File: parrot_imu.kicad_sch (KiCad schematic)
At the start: 1 part

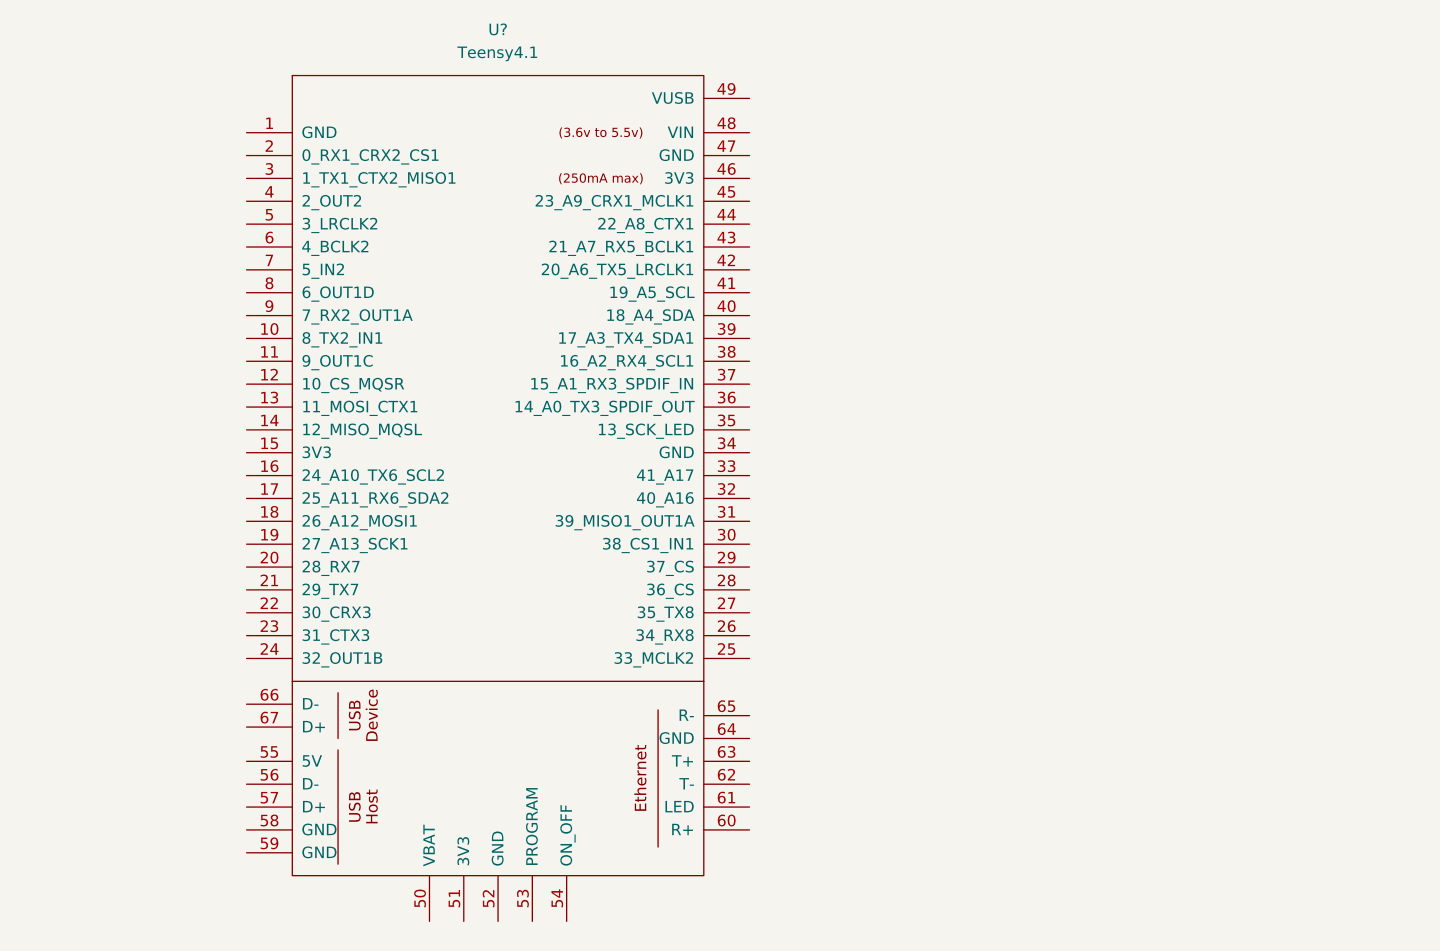
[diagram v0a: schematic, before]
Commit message: added ethernet jack symbol
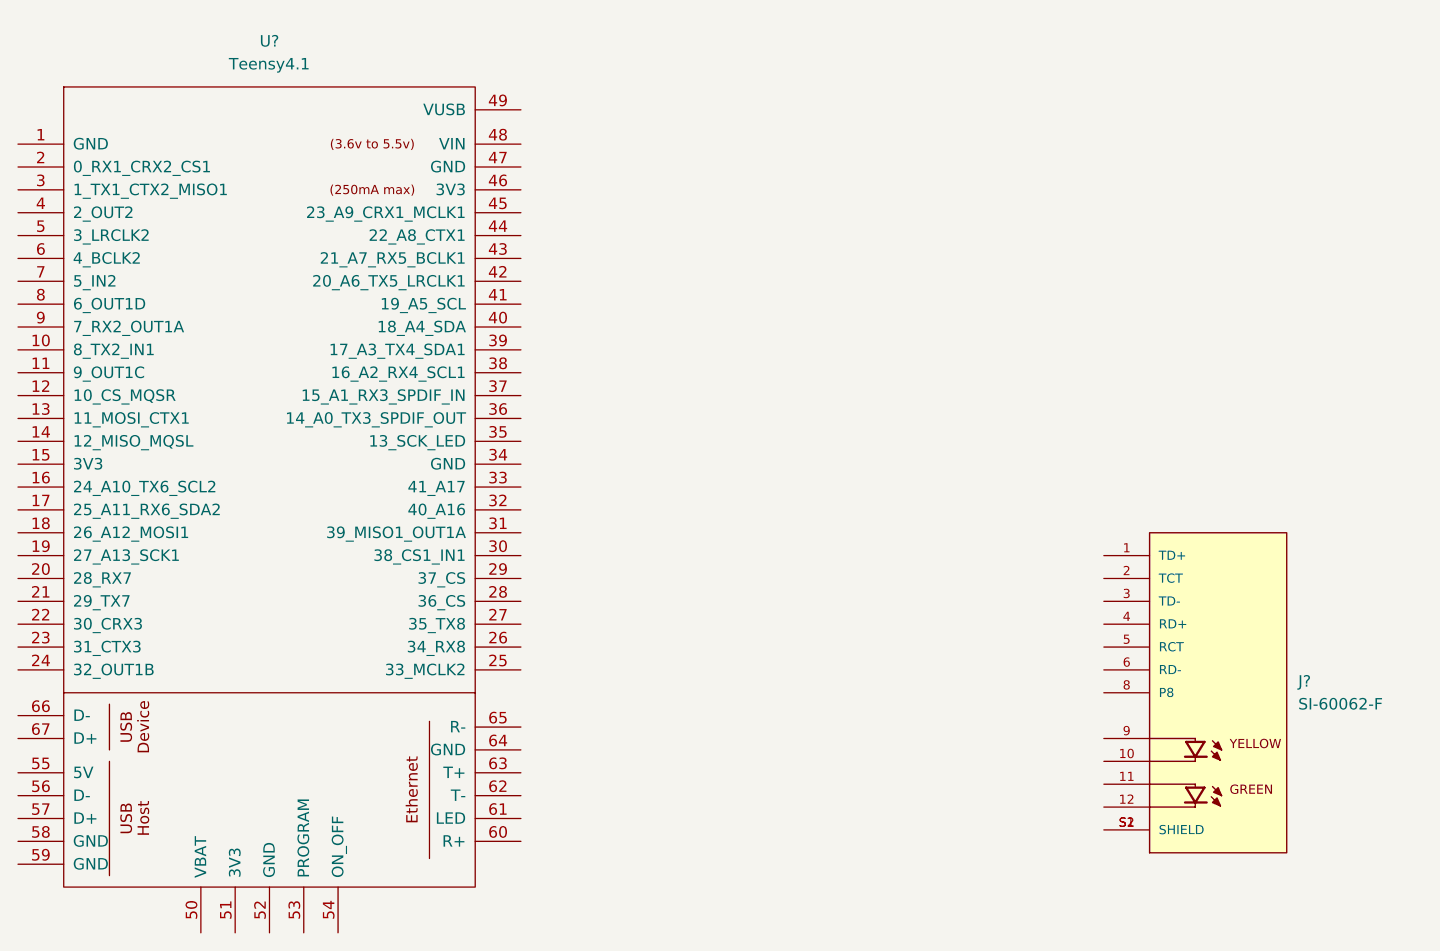
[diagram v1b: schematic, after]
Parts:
- added J?: SI-60062-F, Connector_RJ:RJ45_Bel_SI-60062-F, symbol SI-60062-F:SI-60062-F
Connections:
- new net: J?.S1 (SHIELD), J?.S2 (SHIELD)
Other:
- moved on the sheet: U?
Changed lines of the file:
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@@
 (kicad_sch (version 20211123) (generator eeschema)
   (paper "A4")
-  (symbol (lib_id "teensy_symbol:Teensy4.1") (at 144.78 97.79 0) (unit 1)
+  (symbol (lib_id "teensy_symbol:Teensy4.1") (at 119.38 99.06 0) (unit 1)
     (in_bom yes) (on_board yes) (fields_autoplaced)
-    (property "Reference" "U?" (id 0) (at 144.78 31.75 0))
-    (property "Value" "Teensy4.1" (id 1) (at 144.78 34.29 0))
-    (property "Footprint" "teensy_footprint:Teensy41" (id 2) (at 134.62 87.63 0)
+    (property "Reference" "U?" (id 0) (at 119.38 33.02 0))
+    (property "Value" "Teensy4.1" (id 1) (at 119.38 35.56 0))
+    (property "Footprint" "teensy_footprint:Teensy41" (id 2) (at 109.22 88.9 0)
       (effects (font (size 1.27 1.27)) hide)
     )
-    (property "Datasheet" "" (id 3) (at 134.62 87.63 0)
+    (property "Datasheet" "" (id 3) (at 109.22 88.9 0)
       (effects (font (size 1.27 1.27)) hide)
     )
@@
     (pin "4")
   )
+  (symbol (lib_id "SI-60062-F:SI-60062-F") (at 224.79 105.41 0) (unit 1)
+    (in_bom yes) (on_board yes) (fields_autoplaced)
+    (property "Reference" "J?" (id 0) (at 233.68 104.1399 0)
+      (effects (font (size 1.27 1.27)) (justify left))
+    )
+    (property "Value" "SI-60062-F" (id 1) (at 233.68 106.6799 0)
+      (effects (font (size 1.27 1.27)) (justify left))
+    )
+    (property "Footprint" "Connector_RJ:RJ45_Bel_SI-60062-F" (id 2) (at 224.79 105.41 0)
+      (effects (font (size 1.27 1.27)) (justify bottom) hide)
+    )
+    (property "Datasheet" "" (id 3) (at 224.79 105.41 0)
+      (effects (font (size 1.27 1.27)) hide)
+    )
+    (property "STANDARD" "Manufacturer Recommendations" (id 4) (at 224.79 105.41 0)
+      (effects (font (size 1.27 1.27)) (justify bottom) hide)
+    )
+    (property "MAXIMUM_PACKAGE_HEIGHT" "15.21mm" (id 5) (at 224.79 105.41 0)
+      (effects (font (size 1.27 1.27)) (justify bottom) hide)
+    )
+    (property "MANUFACTURER" "Bel Fuse" (id 6) (at 224.79 105.41 0)
+      (effects (font (size 1.27 1.27)) (justify bottom) hide)
+    )
+    (property "PARTREV" "B0" (id 7) (at 224.79 105.41 0)
+      (effects (font (size 1.27 1.27)) (justify bottom) hide)
+    )
+    (pin "1")
+    (pin "10")
+    (pin "11")
+    (pin "12")
+    (pin "2")
+    (pin "3")
+    (pin "4")
+    (pin "5")
+    (pin "6")
+    (pin "8")
+    (pin "9")
+    (pin "S1")
+    (pin "S2")
+  )
   (sheet_instances
     (path "/" (page "1"))
   )
   (symbol_instances
+    (path "/ee96e4e8-cf28-4230-aa42-258281590056"
+      (reference "J?") (unit 1) (value "SI-60062-F") (footprint "Connector_RJ:RJ45_Bel_SI-60062-F")
+    )
     (path "/cc736701-b530-419e-931a-68b81ff9c957"
       (reference "U?") (unit 1) (value "Teensy4.1") (footprint "teensy_footprint:Teensy41")

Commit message: added digikey part number to ethernet part
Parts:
- J?: Digikey (none) -> 507-SI-60062-F-ND
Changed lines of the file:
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@@
       (effects (font (size 1.27 1.27)) (justify bottom) hide)
+    )
+    (property "Digikey" "507-SI-60062-F-ND" (id 8) (at 224.79 105.41 0)
+      (effects (font (size 1.27 1.27)) hide)
     )
     (pin "1")

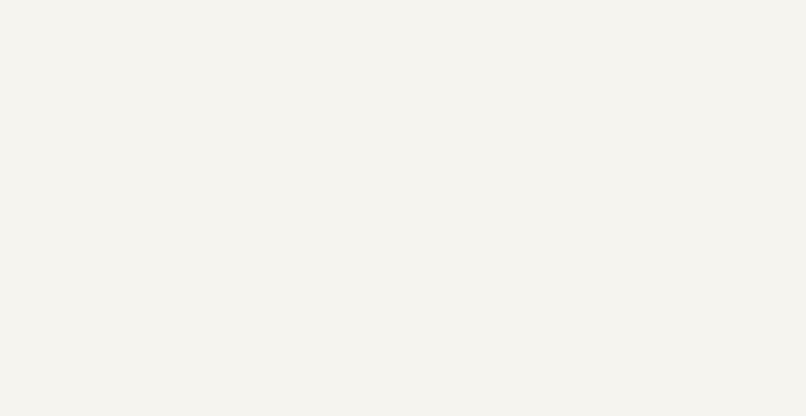
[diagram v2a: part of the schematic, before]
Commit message: created footprint and symbol for ldo
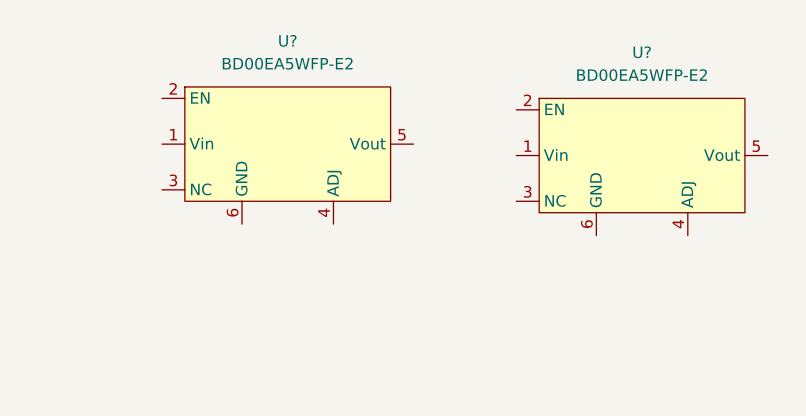
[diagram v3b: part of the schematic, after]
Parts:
- added U? (x2): BD00EA5WFP-E2, parrot_imu:BD00EA5WFP-E2, symbol parrot_imu:BD00EA5WFP-E2
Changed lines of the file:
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@@
 (kicad_sch (version 20211123) (generator eeschema)
   (paper "A4")
+  (symbol (lib_id "parrot_imu:BD00EA5WFP-E2") (at 231.14 46.99 0) (unit 1)
+    (in_bom yes) (on_board yes) (fields_autoplaced)
+    (property "Reference" "U?" (id 0) (at 231.14 35.56 0))
+    (property "Value" "BD00EA5WFP-E2" (id 1) (at 231.14 38.1 0))
+    (property "Footprint" "parrot_imu:BD00EA5WFP-E2" (id 2) (at 231.14 31.75 0)
+      (effects (font (size 1.27 1.27)) hide)
+    )
+    (property "Datasheet" "" (id 3) (at 231.14 46.99 0)
+      (effects (font (size 1.27 1.27)) hide)
+    )
+    (property "Digikey" "846-BD00EA5WFP-E2CT-ND" (id 4) (at 231.14 34.29 0)
+      (effects (font (size 1.27 1.27)) hide)
+    )
+    (pin "1")
+    (pin "2")
+    (pin "3")
+    (pin "4")
+    (pin "5")
+    (pin "6")
+  )
+  (symbol (lib_id "parrot_imu:BD00EA5WFP-E2") (at 191.77 45.72 0) (unit 1)
+    (in_bom yes) (on_board yes) (fields_autoplaced)
+    (property "Reference" "U?" (id 0) (at 191.77 34.29 0))
+    (property "Value" "BD00EA5WFP-E2" (id 1) (at 191.77 36.83 0))
+    (property "Footprint" "parrot_imu:BD00EA5WFP-E2" (id 2) (at 191.77 30.48 0)
+      (effects (font (size 1.27 1.27)) hide)
+    )
+    (property "Datasheet" "" (id 3) (at 191.77 45.72 0)
+      (effects (font (size 1.27 1.27)) hide)
+    )
+    (property "Digikey" "846-BD00EA5WFP-E2CT-ND" (id 4) (at 191.77 33.02 0)
+      (effects (font (size 1.27 1.27)) hide)
+    )
+    (pin "1")
+    (pin "2")
+    (pin "3")
+    (pin "4")
+    (pin "5")
+    (pin "6")
+  )
   (symbol (lib_id "teensy_symbol:Teensy4.1") (at 119.38 99.06 0) (unit 1)
     (in_bom yes) (on_board yes) (fields_autoplaced)
@@
       (reference "J?") (unit 1) (value "SI-60062-F") (footprint "Connector_RJ:RJ45_Bel_SI-60062-F")
     )
+    (path "/77c37afd-a1ed-485e-8b5f-ecf763893ed1"
+      (reference "U?") (unit 1) (value "BD00EA5WFP-E2") (footprint "parrot_imu:BD00EA5WFP-E2")
+    )
+    (path "/9cadbf9f-a3bf-4ef2-ad9b-3cea417c0dcf"
+      (reference "U?") (unit 1) (value "BD00EA5WFP-E2") (footprint "parrot_imu:BD00EA5WFP-E2")
+    )
     (path "/cc736701-b530-419e-931a-68b81ff9c957"

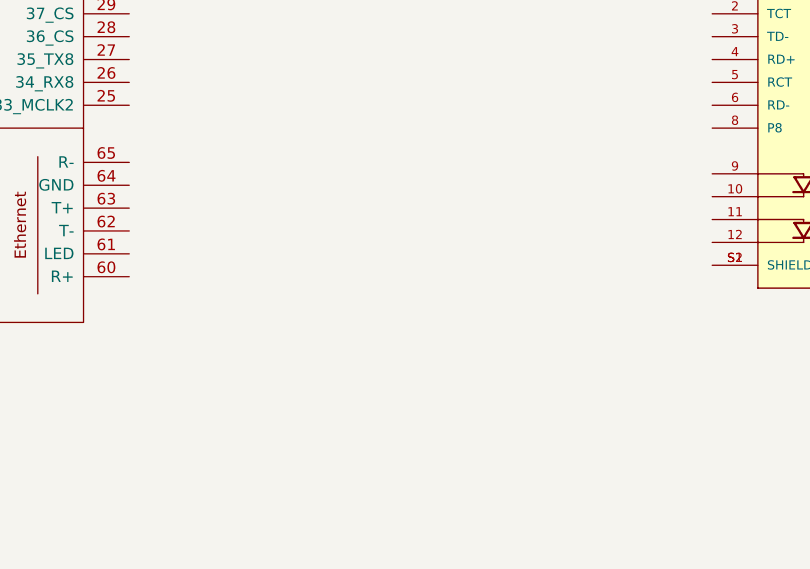
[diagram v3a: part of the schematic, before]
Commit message: added ics to schematic
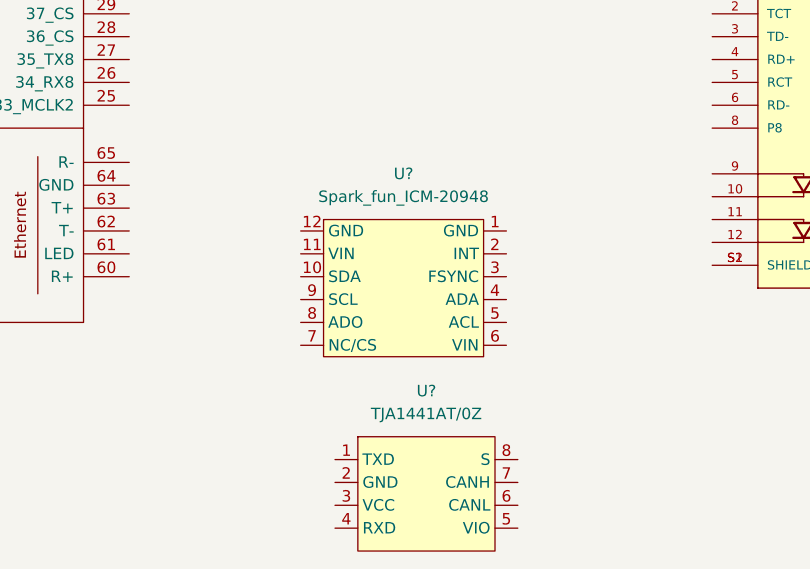
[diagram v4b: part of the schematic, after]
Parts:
- added U?: TJA1441AT/0Z, Package_SO:SO-8_3.9x4.9mm_P1.27mm, symbol parrot_imu:TJA1441AT/0Z
- added U?: Spark_fun_ICM-20948, parrot_imu:Spark_fun_ICM-20498, symbol parrot_imu:Spark_fun_ICM-20948
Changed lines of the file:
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@@
     (pin "6")
+  )
+  (symbol (lib_id "parrot_imu:TJA1441AT{slash}0Z") (at 180.34 146.05 0) (unit 1)
+    (in_bom yes) (on_board yes) (fields_autoplaced)
+    (property "Reference" "U?" (id 0) (at 180.34 134.62 0))
+    (property "Value" "TJA1441AT/0Z" (id 1) (at 180.34 137.16 0))
+    (property "Footprint" "Package_SO:SO-8_3.9x4.9mm_P1.27mm" (id 2) (at 180.34 135.89 0)
+      (effects (font (size 1.27 1.27)) hide)
+    )
+    (property "Datasheet" "" (id 3) (at 180.34 146.05 0)
+      (effects (font (size 1.27 1.27)) hide)
+    )
+    (property "Digikey" "568-TJA1441AT/0ZCT-ND" (id 4) (at 180.34 133.35 0)
+      (effects (font (size 1.27 1.27)) hide)
+    )
+    (pin "1")
+    (pin "2")
+    (pin "3")
+    (pin "4")
+    (pin "5")
+    (pin "6")
+    (pin "7")
+    (pin "8")
   )
   (symbol (lib_id "parrot_imu:BD00EA5WFP-E2") (at 191.77 45.72 0) (unit 1)
@@
     (pin "S2")
   )
+  (symbol (lib_id "parrot_imu:Spark_fun_ICM-20948") (at 177.8 123.19 0) (unit 1)
+    (in_bom yes) (on_board yes) (fields_autoplaced)
+    (property "Reference" "U?" (id 0) (at 177.8 110.49 0))
+    (property "Value" "Spark_fun_ICM-20948" (id 1) (at 177.8 113.03 0))
+    (property "Footprint" "parrot_imu:Spark_fun_ICM-20498" (id 2) (at 177.8 110.49 0)
+      (effects (font (size 1.27 1.27)) hide)
+    )
+    (property "Datasheet" "" (id 3) (at 177.8 123.19 0)
+      (effects (font (size 1.27 1.27)) hide)
+    )
+    (pin "1")
+    (pin "10")
+    (pin "11")
+    (pin "12")
+    (pin "2")
+    (pin "3")
+    (pin "4")
+    (pin "5")
+    (pin "6")
+    (pin "7")
+    (pin "8")
+    (pin "9")
+  )
   (sheet_instances
     (path "/" (page "1"))
@@
       (reference "U?") (unit 1) (value "BD00EA5WFP-E2") (footprint "parrot_imu:BD00EA5WFP-E2")
     )
+    (path "/984f2dfe-4590-479f-8462-472e0a329143"
+      (reference "U?") (unit 1) (value "TJA1441AT/0Z") (footprint "Package_SO:SO-8_3.9x4.9mm_P1.27mm")
+    )
     (path "/9cadbf9f-a3bf-4ef2-ad9b-3cea417c0dcf"
       (reference "U?") (unit 1) (value "BD00EA5WFP-E2") (footprint "parrot_imu:BD00EA5WFP-E2")
@@
       (reference "U?") (unit 1) (value "Teensy4.1") (footprint "teensy_footprint:Teensy41")
     )
-  )
+    (path "/fb147164-c79e-4124-bc0a-41cb012d3ec0"
+      (reference "U?") (unit 1) (value "Spark_fun_ICM-20948") (footprint "parrot_imu:Spark_fun_ICM-20498")
+    )
+  )

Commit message: some progress on the schematic and notes on other things to handle
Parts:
- added C? (x7): C, symbol Device:C
- added R? (x4): R, symbol Device:R
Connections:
- net at U?.1 (Vin): now also U?.2 (EN), C?.1 (x2)
- net at U?.4 (ADJ): now also R?.1, R?.2 (x2)
- net +5V: now reaches U?.5 (Vout)
- net +5V: now also U?.3 (VCC), U?.48 (VIN), C?.1, C?.1, R?.1
- net GND: now reaches U?.6 (GND)
- net GND: now also J?.10, J?.5 (RCT), J?.8 (P8), U?.1 (GND), U?.1 (GND), U?.12 (GND), U?.2 (GND), U?.34 (GND), U?.47 (GND), U?.6 (GND), U?.64 (GND), U?.8 (S), C?.2, C?.2, C?.2, C?.2, C?.2, C?.2, C?.2, R?.2, R?.2
- net Can_tx: now reaches U?.1 (TXD)
- net Can_tx: now also U?.44 (22_A8_CTX1)
- net Can_rx: now reaches U?.4 (RXD)
- net Can_rx: now also U?.45 (23_A9_CRX1_MCLK1)
- net +3.3V: now reaches U?.5 (VIO)
- net +3.3V: now also U?.11 (VIN), U?.15 (3V3), U?.46 (3V3), U?.5 (Vout), U?.6 (VIN), C?.1, C?.1, R?.1
- net Eth_rx+: now reaches U?.60 (R+)
- net Eth_rx+: now also J?.4 (RD+)
- net Eth_led: now reaches U?.61 (LED)
- net Eth_led: now also J?.9
- net Eth_tx-: now reaches U?.62 (T-)
- net Eth_tx-: now also J?.3 (TD-)
- net Eth_tx+: now reaches U?.63 (T+)
- net Eth_tx+: now also J?.1 (TD+)
- net Eth_rx-: now reaches U?.65 (R-)
- net Eth_rx-: now also J?.6 (RD-)
- net at J?.2 (TCT): now also C?.1
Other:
- note added: "Do I need to chuck on a couple of diodes or something here like with older teensies?"
- note added: "Need to find and add a connector here for CAN I/O."
- note added: "Need to find and add a connector here for power input. This should be nominally in the range of 24-21V but this is worth checking. VBat can also go straight to the enable pins on these chips. The schematic suggests some simple reverse polarity protection by adding a fet and diode. Consider this and ask tony."
- moved on the sheet: J?, U?

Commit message: schematic done pre review
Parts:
- removed C? (x4): C, symbol Device:C
- removed R? (x4): R, symbol Device:R
- removed U? (x2): BD00EA5WFP-E2, parrot_imu:BD00EA5WFP-E2, symbol parrot_imu:BD00EA5WFP-E2
- added C? (x2): 22uF, symbol Device:C_Polarized
- added C?: 47uF, symbol Device:C_Polarized
- added C?: 10uF, symbol Device:C_Polarized
- added J? (x2): TB005-762-02BE, connector_parrot:CUI_TB005-762-02BE, symbol connector_parrot:TB005-762-02BE
- added R? (x2): 60, symbol Device:R
- added U?: TR05S3V3, parrot_imu:TR05S3V3, symbol parrot_imu:TR05S3V3
- added U?: VR10S05, parrot_imu:VR10S05, symbol parrot_imu:VR10S05
- C? (x3): value C -> 0.1uF
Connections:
- net +3.3V: now also C?.1, U?.3 (Vout)
- net +5V: now also C?.1, U?.3 (Vout)
- net GND: now also C?.2, C?.2, C?.2, C?.2, J?.2, R?.1, R?.2, U?.2 (GND), U?.2 (GND)
- net at U?.6 (CANL): now also J?.2, R?.2
- net at U?.7 (CANH): now also J?.1, R?.1
- net MOSI: now reaches U?.18 (26_A12_MOSI1)
- net MOSI: now also U?.10 (MOSI)
- net SCK: now reaches U?.19 (27_A13_SCK1)
- net SCK: now also U?.9 (SCK)
- net CS: now reaches U?.2 (0_RX1_CRX2_CS1)
- net CS: now also U?.7 (!CS)
- net MISO: now reaches U?.3 (1_TX1_CTX2_MISO1)
- net MISO: now also U?.8 (MISO)
- new net: C?.1, C?.1, J?.1, U?.1 (Vin), U?.1 (Vin)
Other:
- note added: "10μF/50V"
- note added: "22μF/10V"
- note added: "No notes on voltage rating for these so I guess just match it?"
- note removed: "Need to find and add a connector here for power input. This should be nominally in the range of 24-21V but this is worth checking. VBat can also go straight to the enable pins on these chips. The schematic suggests some simple reverse polarity protection by adding a fet and diode. Consider this and ask tony."
- moved on the sheet: C?, J?, U?

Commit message: added notes and digikey part numbers
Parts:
- J? (x2): Digikey (none) -> 102-6189-ND
- U?: Digikey (none) -> 1470-2257-5-ND
- U?: Digikey (none) -> 1470-VR10S05-ND
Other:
- note added: "Shottkey Diode for protection?"
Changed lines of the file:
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@@
+    (effects (font (size 1.27 1.27)) (justify left bottom))
+  )
+  (text "Shottkey Diode for protection?" (at 21.59 110.49 0)
     (effects (font (size 1.27 1.27)) (justify left bottom))
   )
@@
     )
     (property "Datasheet" "" (id 3) (at 74.93 127 0)
+      (effects (font (size 1.27 1.27)) hide)
+    )
+    (property "Digikey" "1470-2257-5-ND" (id 4) (at 74.93 127 0)
       (effects (font (size 1.27 1.27)) hide)
     )
@@
       (effects (font (size 1.27 1.27)) (justify bottom) hide)
     )
+    (property "Digikey" "102-6189-ND" (id 6) (at 29.21 129.54 0)
+      (effects (font (size 1.27 1.27)) hide)
+    )
     (pin "1")
     (pin "2")
@@
     (property "STANDARD" "Manufacturer Recommendations" (id 5) (at 363.22 82.55 0)
       (effects (font (size 1.27 1.27)) (justify bottom) hide)
+    )
+    (property "Digikey" "102-6189-ND" (id 6) (at 363.22 82.55 0)
+      (effects (font (size 1.27 1.27)) hide)
     )
     (pin "1")
@@
       (effects (font (size 1.27 1.27)) hide)
     )
+    (property "Digikey" "1470-VR10S05-ND" (id 4) (at 74.93 156.21 0)
+      (effects (font (size 1.27 1.27)) hide)
+    )
